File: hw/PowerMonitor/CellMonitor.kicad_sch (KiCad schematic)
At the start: 25 parts, among them Q1 Q_PMOS_GDS, U5 LM358, U6 LM358, U7 LM358, U8 LM393, U9 74LVC1G32

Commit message: Rework powermon
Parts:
- removed C10: 33n, Capacitor_SMD:C_0603_1608Metric_Pad1.08x0.95mm_HandSolder, symbol Device:C
- removed C11, C12, C13: 1u, Capacitor_SMD:C_0603_1608Metric_Pad1.08x0.95mm_HandSolder, symbol Device:C
- removed D2, D3: BZT52Bxx, Diode_SMD:D_SOD-123F, symbol Diode:BZT52Bxx
- removed Q1: Q_PMOS_GDS, Package_TO_SOT_SMD:TO-252-2, symbol Transistor_FET:Q_PMOS_GDS
- removed R11, R8, R9: 1k, Resistor_SMD:R_0603_1608Metric_Pad0.98x0.95mm_HandSolder, symbol Device:R
- removed R12: 5.6k, Resistor_SMD:R_0603_1608Metric_Pad0.98x0.95mm_HandSolder, symbol Device:R
- removed R13: 1.8k, Resistor_SMD:R_0603_1608Metric_Pad0.98x0.95mm_HandSolder, symbol Device:R
- removed R14, R15: 150, Resistor_SMD:R_0603_1608Metric_Pad0.98x0.95mm_HandSolder, symbol Device:R
- removed R16: 16k, Resistor_SMD:R_0603_1608Metric_Pad0.98x0.95mm_HandSolder, symbol Device:R
- removed R17: 2k, Resistor_SMD:R_0603_1608Metric_Pad0.98x0.95mm_HandSolder, symbol Device:R
- removed R18, R19: 4.7k, Resistor_SMD:R_0603_1608Metric_Pad0.98x0.95mm_HandSolder, symbol Device:R
- removed U5, U6, U7: LM358, Package_SO:SOIC-8_3.9x4.9mm_P1.27mm, symbol Amplifier_Operational:LM358
- removed U8: LM393, Package_SO:SOIC-8_3.9x4.9mm_P1.27mm, symbol Comparator:LM393
- removed U9: 74LVC1G32, Package_TO_SOT_SMD:SOT-353_SC-70-5_Handsoldering, symbol 74xGxx:74LVC1G32
- added C23: 33n, Capacitor_SMD:C_0603_1608Metric_Pad1.08x0.95mm_HandSolder, symbol Device:C
- added C26, C29: 1u, Capacitor_SMD:C_0603_1608Metric_Pad1.08x0.95mm_HandSolder, symbol Device:C
- added D10, D13: BZT52Bxx, Diode_SMD:D_SOD-123F, symbol Diode:BZT52Bxx
- added D2: BAT54C, Package_TO_SOT_SMD:SOT-23_Handsoldering, symbol Diode:BAT54C
- added Q4: Q_PMOS_GDS, Package_TO_SOT_SMD:TO-252-2, symbol Transistor_FET:Q_PMOS_GDS
- added R48: 1k, Resistor_SMD:R_0603_1608Metric_Pad0.98x0.95mm_HandSolder, symbol Device:R
- added R51: 5.6k, Resistor_SMD:R_0603_1608Metric_Pad0.98x0.95mm_HandSolder, symbol Device:R
- added R52: 16k, Resistor_SMD:R_0603_1608Metric_Pad0.98x0.95mm_HandSolder, symbol Device:R
- added R57: 1.8k, Resistor_SMD:R_0603_1608Metric_Pad0.98x0.95mm_HandSolder, symbol Device:R
- added R58: 2k, Resistor_SMD:R_0603_1608Metric_Pad0.98x0.95mm_HandSolder, symbol Device:R
- added R?: 0R, Resistor_SMD:R_0603_1608Metric_Pad0.98x0.95mm_HandSolder, symbol Device:R
- added R? (x2): 150, Resistor_SMD:R_0603_1608Metric_Pad0.98x0.95mm_HandSolder, symbol Device:R
- added U16, U5: LM358, Package_SO:SOIC-8_3.9x4.9mm_P1.27mm, symbol Amplifier_Operational:LM358
- added U19: LM393, Package_SO:SOIC-8_3.9x4.9mm_P1.27mm, symbol Comparator:LM393
- R10, R7: value 1k -> 10k
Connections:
- net GND: now also R10.2, R7.2, C26.1, C29.1, U19.4 (V-)
- net VbatH: now also Q4.2 (D)
- net VbatL: now also D10.2 (A), D13.2 (A), R48.2, R52.1, R58.1, U5.4 (V-), U5.5 (+), U5.6 (-); no longer R7.2
- net Vlogic: now also C26.2, C29.2, U19.8 (V+), U5.8 (V+)
- net Vprot: now also C23.2, Q4.3 (S), U16.3 (+)
- net UNDERVOLTAGE: now reaches R7.1
- net UNDERVOLTAGE: now also D2.2, U19.1
- net GNDREF renamed OVERVOLTAGE
- net OVERVOLTAGE: now also D2.1, U19.7
- new net: R51.2, R57.2, R?.1, R?.1, R?.1, U16.1
- new net: R?.2, U16.2 (-)
- new net: R57.1, R58.2, U19.5 (+)
- new net: D13.1 (K), R?.2, U19.6 (-)
- new net: C23.1, Q4.1 (G), R48.1
- new net: R51.1, R52.2, U19.2 (-)
- new net: D10.1 (K), R?.2, U19.3 (+)
- new net UVOV: D2.3
- no-connect marks 3 -> 1

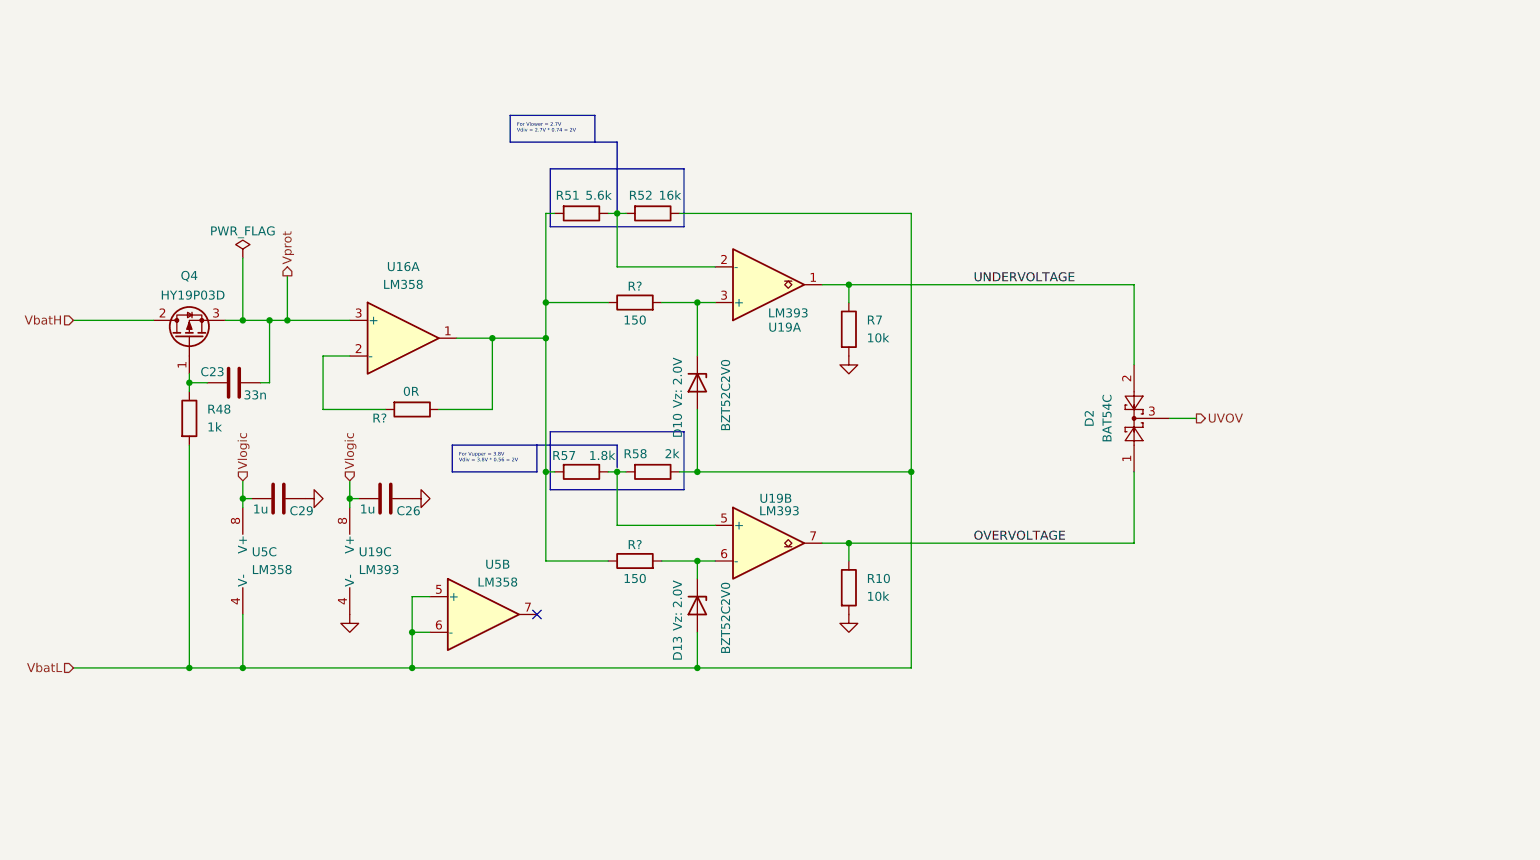
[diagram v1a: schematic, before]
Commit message: ad uvov in powermon, overcurrent and prepare for latch alarm
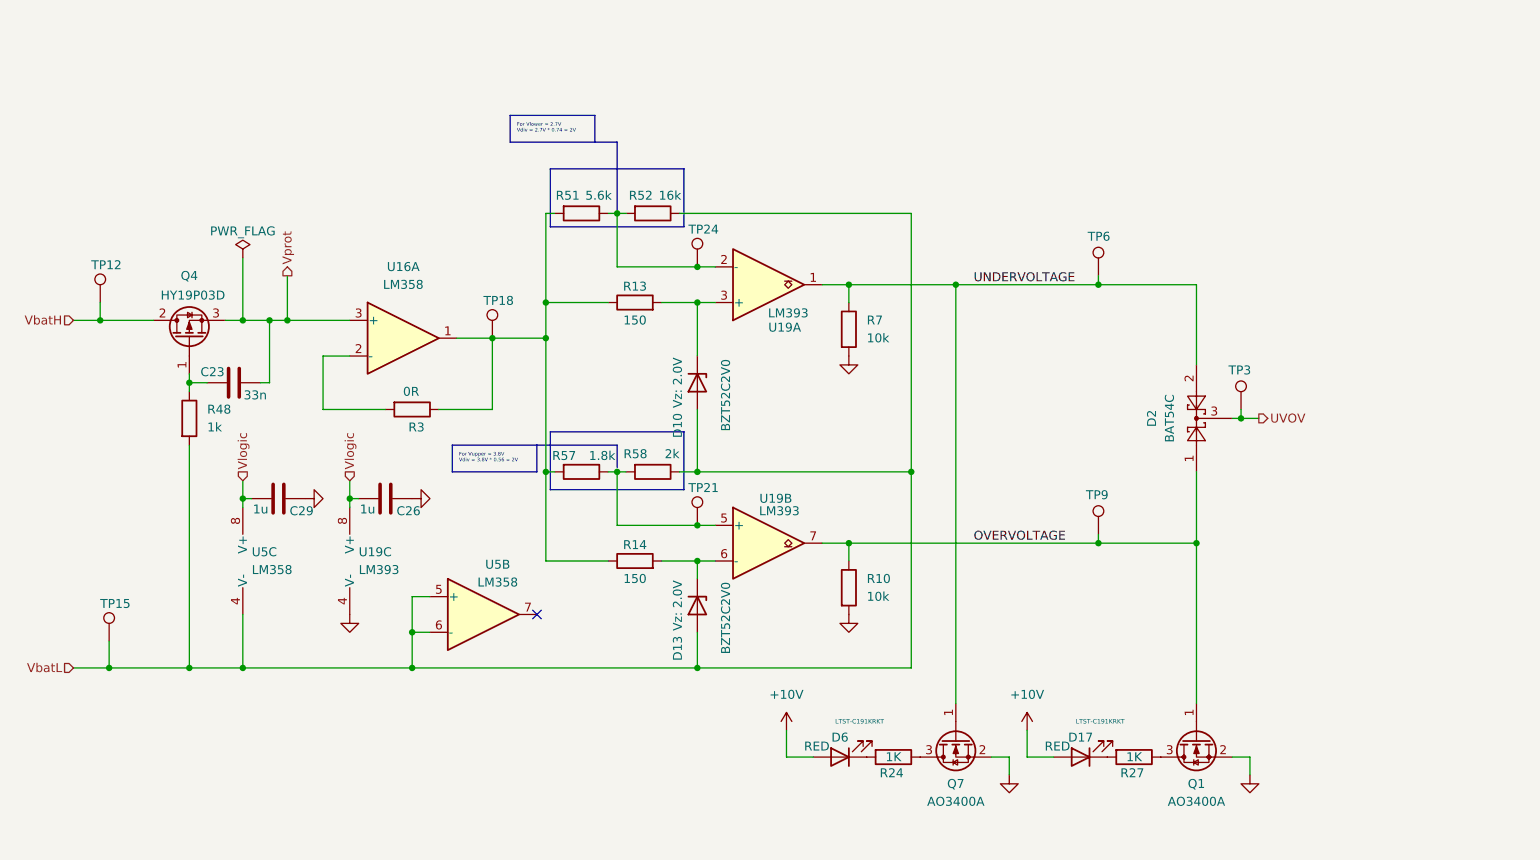
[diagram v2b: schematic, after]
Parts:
- added D17, D6: RED, LED_SMD:LED_0603_1608Metric, symbol Device:LED
- added Q1, Q7: AO3400A, Package_TO_SOT_SMD:SOT-23_Handsoldering, symbol Transistor_FET:AO3400A
- added R24, R27: 1K, Resistor_SMD:R_0603_1608Metric, symbol Device:R
- added TP12, TP15, TP18, TP21, TP24, TP3, TP6, TP9: TestPoint, Connector_Pin:Pin_D1.4mm_L8.5mm_W2.8mm_FlatFork, symbol Connector:TestPoint
- gave numbers to parts that had none: 3
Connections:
- net GND: now also Q1.2 (S), Q7.2 (S)
- net OVERVOLTAGE: now also Q1.1 (G), TP9.1
- net UNDERVOLTAGE: now also Q7.1 (G), TP6.1
- net UVOV: now also TP3.1
- net VbatH: now also TP12.1
- net VbatL: now also TP15.1
- net at R13.1, R14.1, R3.1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: now also TP18.1
- net at R57.1, R58.2, U19.5 (+): now also TP21.1
- net at R51.1, R52.2, U19.2 (-): now also TP24.1
- new net: D6.1 (K), R24.2
- new net: D17.1 (K), R27.2
- new net: Q1.3 (D), R27.1
- new net: Q7.3 (D), R24.1
- new net +10V: D17.2 (A), D6.2 (A)
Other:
- moved on the sheet: D2

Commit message: * hw/PowerMonitor/CellMonitor.kicad_sch: start PCB layout
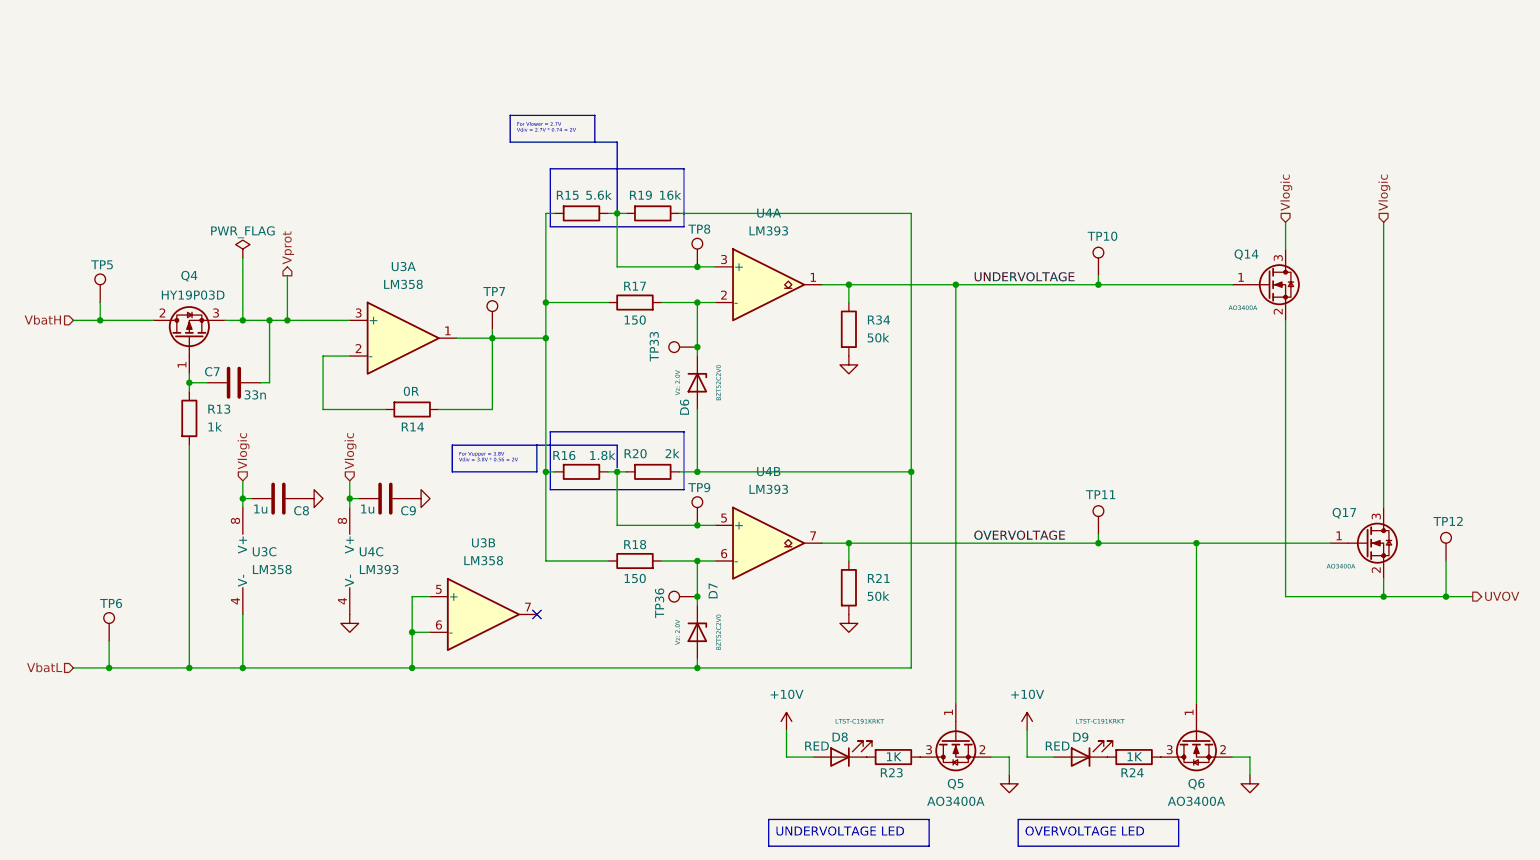
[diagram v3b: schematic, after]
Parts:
- removed D2: BAT54C, Package_TO_SOT_SMD:SOT-23_Handsoldering, symbol Diode:BAT54C
- removed R10, R7: 10k, Resistor_SMD:R_0603_1608Metric_Pad0.98x0.95mm_HandSolder, symbol Device:R
- removed U16, U5: LM358, Package_SO:SOIC-8_3.9x4.9mm_P1.27mm, symbol Amplifier_Operational:LM358
- removed U19: LM393, Package_SO:SOIC-8_3.9x4.9mm_P1.27mm, symbol Comparator:LM393
- added Q14, Q17: AO3400A, Package_TO_SOT_SMD:SOT-23_Handsoldering, symbol Transistor_FET:AO3400A
- added R21, R34: 50k, Resistor_SMD:R_0603_1608Metric_Pad0.98x0.95mm_HandSolder, symbol Device:R
- added TP33, TP36: TestPoint, TestPoint:TestPoint_Pad_1.0x1.0mm, symbol Connector:TestPoint
- added U3: LM358, Package_SO:SOIC-8_3.9x4.9mm_P1.27mm, symbol Amplifier_Operational:LM358
- added U4: LM393, Package_SO:SOIC-8_3.9x4.9mm_P1.27mm, symbol Comparator:LM393
- TP10: renamed from TP6; footprint Connector_Pin:Pin_D1.4mm_L8.5mm_W2.8mm_FlatFork -> TestPoint:TestPoint_Pad_1.0x1.0mm
- TP11: renamed from TP9; footprint Connector_Pin:Pin_D1.4mm_L8.5mm_W2.8mm_FlatFork -> TestPoint:TestPoint_Pad_1.0x1.0mm
- TP12: renamed from TP3; footprint Connector_Pin:Pin_D1.4mm_L8.5mm_W2.8mm_FlatFork -> TestPoint:TestPoint_Pad_1.0x1.0mm
- TP5: renamed from TP12; footprint Connector_Pin:Pin_D1.4mm_L8.5mm_W2.8mm_FlatFork -> TestPoint:TestPoint_Pad_1.0x1.0mm
- TP6: renamed from TP15; footprint Connector_Pin:Pin_D1.4mm_L8.5mm_W2.8mm_FlatFork -> TestPoint:TestPoint_Pad_1.0x1.0mm
- TP7: renamed from TP18; footprint Connector_Pin:Pin_D1.4mm_L8.5mm_W2.8mm_FlatFork -> TestPoint:TestPoint_Pad_1.0x1.0mm
- TP8: renamed from TP24; footprint Connector_Pin:Pin_D1.4mm_L8.5mm_W2.8mm_FlatFork -> TestPoint:TestPoint_Pad_1.0x1.0mm
- TP9: renamed from TP21; footprint Connector_Pin:Pin_D1.4mm_L8.5mm_W2.8mm_FlatFork -> TestPoint:TestPoint_Pad_1.0x1.0mm
- renumbered C23 to C7, C29 to C8, C26 to C9, D10 to D6, D13 to D7, D6 to D8, D17 to D9, Q7 to Q5, Q1 to Q6, R48 to R13, R3 to R14, R51 to R15, R57 to R16, R13 to R17, R14 to R18, R52 to R19, R58 to R20, R24 to R23, R27 to R24
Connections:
- net GND: now also R21.2, R34.2, U4.4 (V-)
- net OVERVOLTAGE: now also Q17.1 (G), R21.1, U4.7
- net UNDERVOLTAGE: now also Q14.1 (G), R34.1, U4.1
- net UVOV: now also Q14.2 (S), Q17.2 (S)
- net VbatL: now also U3.4 (V-), U3.5 (+), U3.6 (-)
- net Vlogic: now also Q14.3 (D), Q17.3 (D), U3.8 (V+), U4.8 (V+)
- net Vprot: now also U3.3 (+)
- net at R14.1, R15.2, R16.2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: now also U3.1
- net at R14.2: now also U3.2 (-)
- net at R16.1, R20.2, TP9.1: now also U4.5 (+)
- net at D7.1 (K), R18.2: now also TP36.1, U4.6 (-)
- net at R15.1, R19.2, TP8.1: now also U4.3 (+)
- net at D6.1 (K), R17.2: now also TP33.1, U4.2 (-)
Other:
- moved on the sheet: D7, TP12, TP7

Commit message: finish PowerMonitor placement
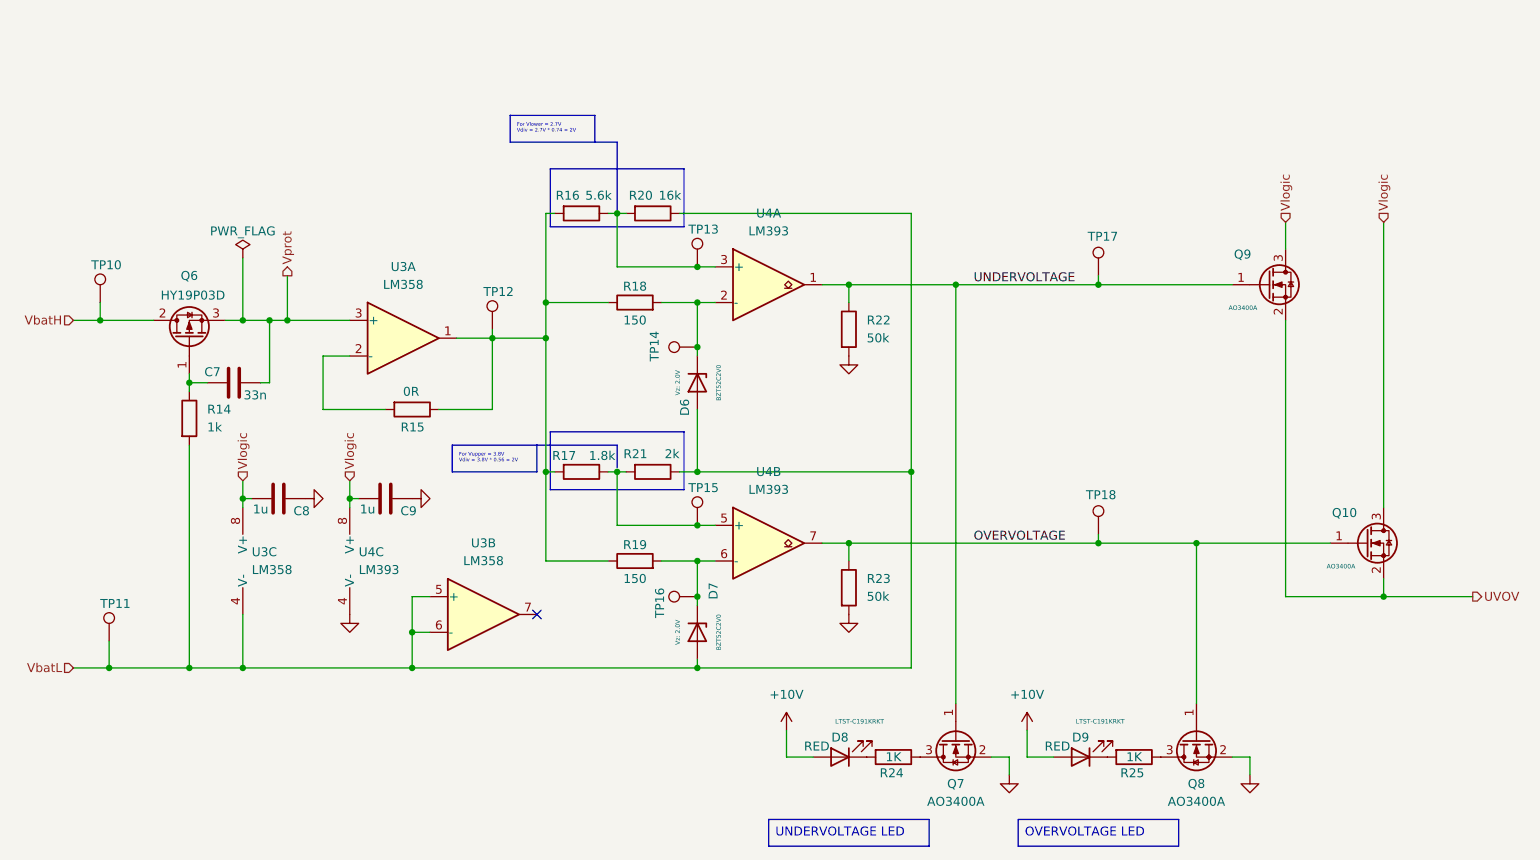
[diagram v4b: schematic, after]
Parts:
- removed R23: 1K, Resistor_SMD:R_0603_1608Metric, symbol Device:R
- removed TP12: TestPoint, TestPoint:TestPoint_Pad_1.0x1.0mm, symbol Connector:TestPoint
- added R24: 1K, Resistor_SMD:R_0603_1608Metric_Pad0.98x0.95mm_HandSolder, symbol Device:R
- R25: renamed from R24; footprint Resistor_SMD:R_0603_1608Metric -> Resistor_SMD:R_0603_1608Metric_Pad0.98x0.95mm_HandSolder
- renumbered Q17 to Q10, Q4 to Q6, Q5 to Q7, Q6 to Q8, Q14 to Q9, R13 to R14, R14 to R15, R15 to R16, R16 to R17, R17 to R18, R18 to R19, R19 to R20, R20 to R21, R34 to R22, R21 to R23, TP5 to TP10, TP6 to TP11, TP7 to TP12, TP8 to TP13, TP33 to TP14, TP9 to TP15, TP36 to TP16, TP10 to TP17, TP11 to TP18
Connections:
- net at D8.1 (K): now also R24.2
- net at Q7.3 (D): now also R24.1

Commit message: remote_ctrl: start working on it
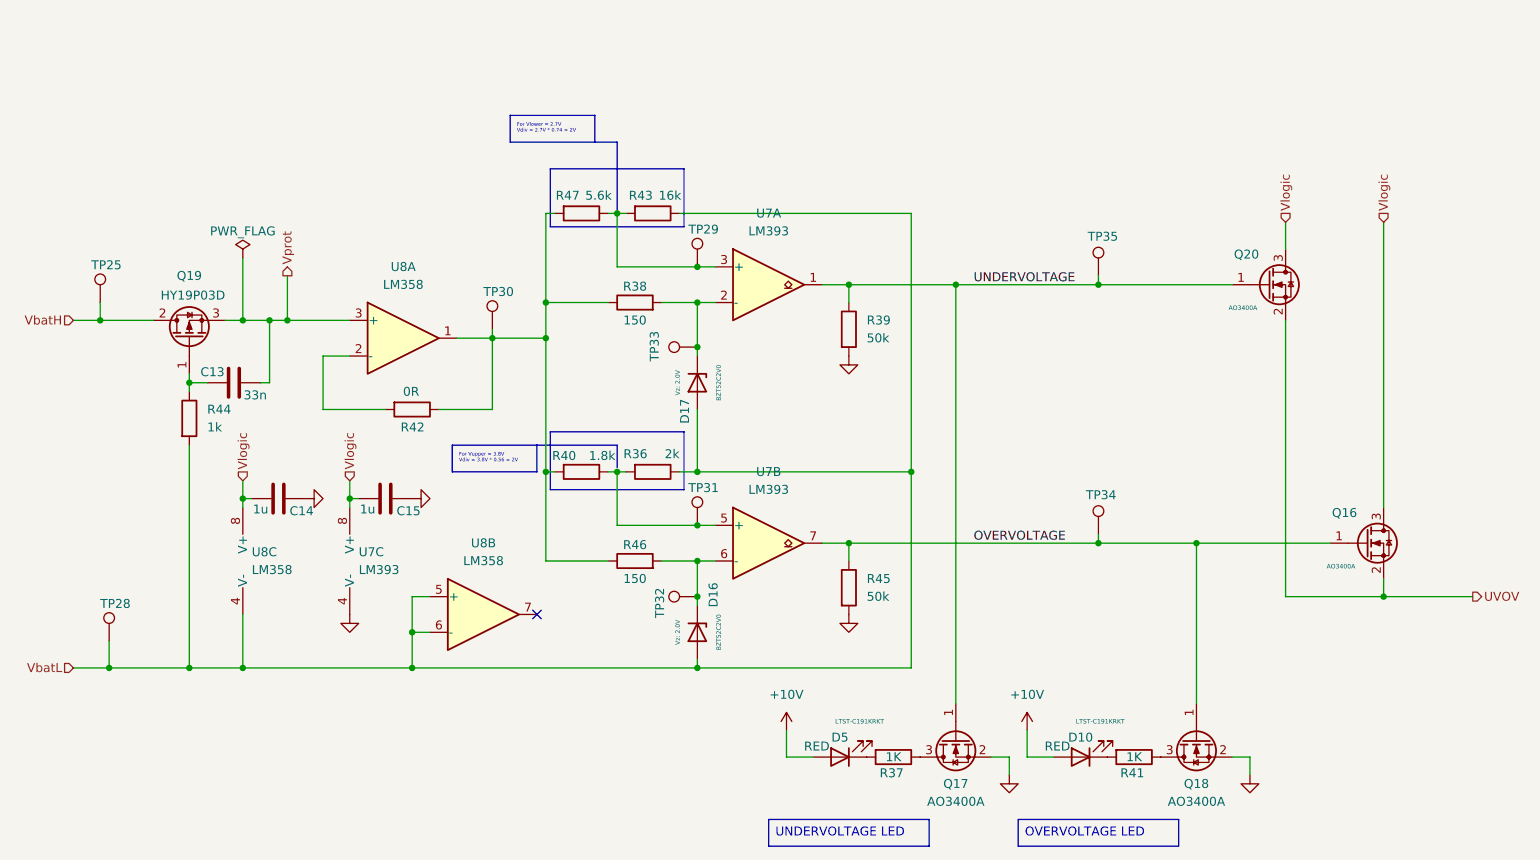
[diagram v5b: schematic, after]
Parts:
- renumbered C7 to C13, C8 to C14, C9 to C15, D9 to D10, D7 to D16, D6 to D17, D8 to D5, Q10 to Q16, Q7 to Q17, Q8 to Q18, Q6 to Q19, Q9 to Q20, R21 to R36, R24 to R37, R18 to R38, R22 to R39, R17 to R40, R25 to R41, R15 to R42, R20 to R43, R14 to R44, R23 to R45, R19 to R46, R16 to R47, TP10 to TP25, TP11 to TP28, TP13 to TP29, TP12 to TP30, TP15 to TP31, TP16 to TP32, TP14 to TP33, TP18 to TP34, TP17 to TP35, U4 to U7, U3 to U8
